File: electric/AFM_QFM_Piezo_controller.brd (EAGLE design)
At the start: 63.2 x 55.9 mm, 42 parts, among them U1 LTC3260EMSE#PBF, U2 AD5696RARUZ-RL7RU_16_ADI-M, U3 LM324KAD

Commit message: allboards
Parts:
- added C10, C12, C8: 10uF, SparkFun-Capacitors:0805
- added C11, C13, C9: 0.1uF, eagle-ltspice:C0805
- moved R8 6.35 mm to (33.0, 20.3)
- moved R9 6.35 mm to (29.2, 20.3)
- moved R18 5.24 mm to (22.9, 30.5)
- moved U$3 2.84 mm to (30.5, 25.4), turned to 90 degrees
- moved U$4 2.84 mm to (34.3, 25.4), turned to 90 degrees
- moved J2 2.54 mm to (2.54, 38.1)
- moved C2 1.27 mm to (39.4, 40.6)
- moved R1 1.27 mm to (48.3, 27.9)
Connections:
- removed net GROUND: C7.2, R4.1, U2.4
- removed net N$5: C2.2, J1.2, U1.1, U1.11, U1.13
- removed net VCC: C6.1, R3.2, U1.5, U3.11
- new net LDO+: C7.1, C8.1, C9.1, R14.2, R2.2, U1.12, U3.4
- new net LDO-: C10.1, C11.1, C6.1, R3.2, U1.5, U3.11
- net AGND: now also B1.GND@0, B1.GND@1, B1.GND@2, C10.2, C11.2, C12.2, C13.2, C7.2, C8.2, C9.2, J1.1, R4.1, U2.4; no longer J1.3, U2.10
- net VDD: now also C12.1, C13.1, C2.2, J1.2, U1.1, U1.11, U1.13, U2.10; no longer C7.1, R14.2, R2.2, U1.12, U3.4
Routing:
- net LDO-: track 0.00 -> 77.8 mm, vias 0 -> 2
- net VCC: track 69.7 -> 0.00 mm, vias 2 -> 0
- net N$5: track 48.3 -> 0.00 mm, vias 3 -> 0
- net LDO+: track 0.00 -> 38.1 mm, vias 0 -> 2
- net AGND: track 2.40 -> 27.1 mm, vias 0 -> 3
- net VDD: track 88.1 -> 98.2 mm, vias 3 -> 4
- net N$19: track 21.4 -> 28.5 mm
- net N$22: track 22.3 -> 27.4 mm
- net LDAC: track 34.2 -> 38.2 mm, vias 0 -> 2
- net VOUTB: track 16.9 -> 14.3 mm
- net P_OUT3: track 10.8 -> 13.3 mm
- net P_OUT4: track 29.1 -> 31.6 mm
- net N$24: track 8.44 -> 10.7 mm
- net N$2: track 3.81 -> 5.50 mm
- net N$9: track 9.67 -> 11.1 mm
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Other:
- board size 63.2 x 55.9 mm -> 64.4 x 55.9 mm

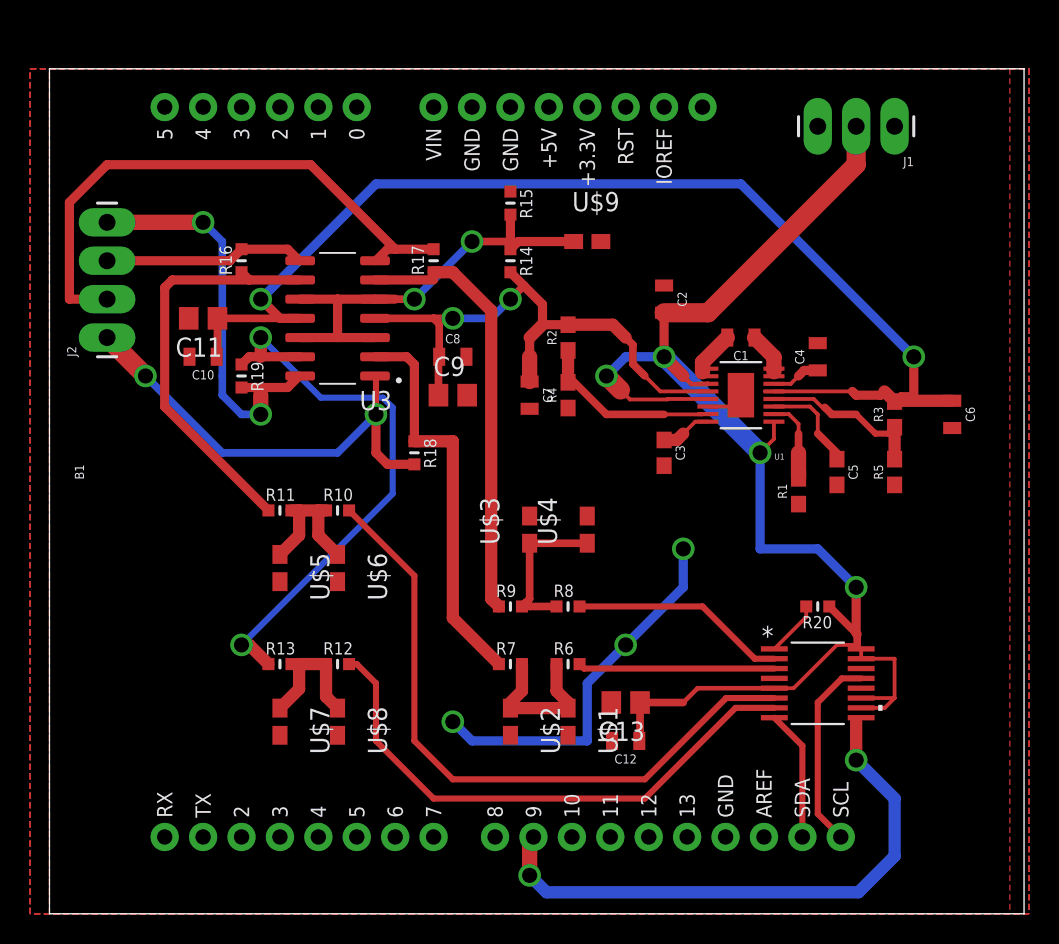
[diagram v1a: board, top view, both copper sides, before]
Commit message: Charge pump with his own power source
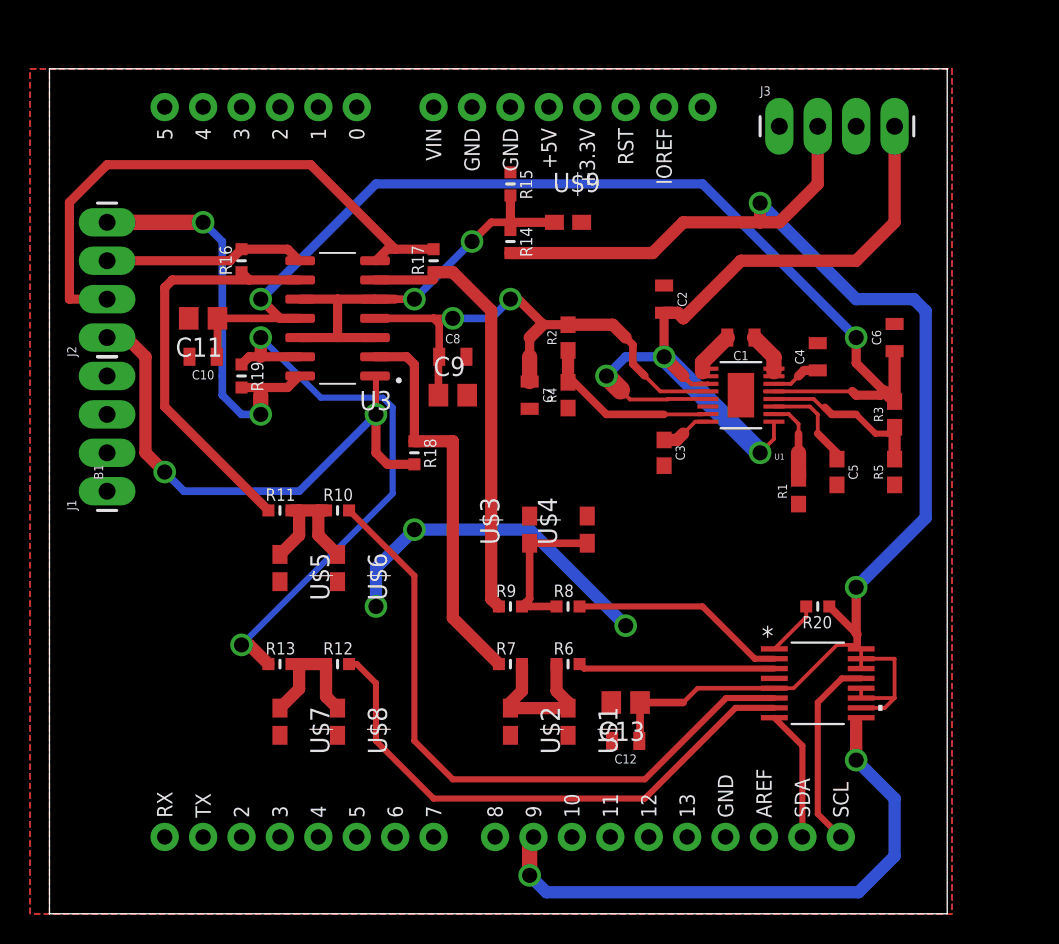
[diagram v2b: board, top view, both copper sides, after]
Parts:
- added J3: (no value), SparkFun-Connectors:1X04_LONGPADS
- J1: device SparkFun-Connectors:1X03_LONGPADS -> SparkFun-Connectors:1X04_LONGPADS
- moved J1 57.4 mm to (2.54, 27.9), turned to 90 degrees
- moved C6 6.35 mm to (54.6, 38.1), turned to 90 degrees
- moved U$9 1.80 mm to (33.0, 45.7)
- moved R14 1.27 mm to (29.2, 44.5)
- moved R15 1.27 mm to (29.2, 48.3)
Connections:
- new net V15+: C2.2, J3.4, U1.1, U1.11, U1.13
- net AGND: now also J1.2, J1.3, J1.4, J3.1; no longer U2.12, U2.14
- net LDO+: no longer R14.2
- net VDD: now also J3.2, R14.2, U2.12, U2.14; no longer C2.2, J1.2, U1.1, U1.11, U1.13
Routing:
- net V15+: track 0.00 -> 52.8 mm, vias 0 -> 3
- net P_OUT1: track 30.0 -> 35.8 mm
- net AGND: track 27.1 -> 22.7 mm
- net LDO-: track 77.8 -> 74.3 mm
- net LDO+: track 38.1 -> 35.6 mm
- net V_REF: track 29.3 -> 28.3 mm
- net N$3: track 2.79 -> 3.29 mm
- net VDD: track 98.2 -> 98.1 mm, vias 4 -> 2
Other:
- board size 64.4 x 55.9 mm -> 59.4 x 55.9 mm

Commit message: newer electroincs
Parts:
- J1: device SparkFun-Connectors:1X04_LONGPADS -> SparkFun-Connectors:1X01_LONGPAD
- moved J1 7.62 mm to (2.54, 35.6)
- moved J3 7.62 mm to (54.6, 52.1), turned to 180 degrees
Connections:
- net AGND: no longer J1.2, J1.3, J1.4
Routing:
- net V15+: track 52.8 -> 68.4 mm
- net VDD: track 98.1 -> 99.2 mm
- net N$22: track 27.4 -> 27.9 mm, vias 0 -> 1
- net N$16: track 26.4 -> 26.8 mm, vias 0 -> 1
- net N$19: vias 0 -> 1
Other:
- board size 59.4 x 55.9 mm -> 59.4 x 58.4 mm
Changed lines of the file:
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@@
 <plain>
 <wire x1="-1.27" y1="0" x2="58.09" y2="0" width="0" layer="20"/>
-<wire x1="58.09" y1="0" x2="58.09" y2="55.87" width="0" layer="20"/>
-<wire x1="58.09" y1="55.87" x2="-1.27" y2="55.87" width="0" layer="20"/>
-<wire x1="-1.27" y1="55.87" x2="-1.27" y2="0" width="0" layer="20"/>
+<wire x1="58.09" y1="0" x2="58.09" y2="58.41" width="0" layer="20"/>
+<wire x1="58.09" y1="58.41" x2="-1.27" y2="58.41" width="0" layer="20"/>
+<wire x1="-1.27" y1="58.41" x2="-1.27" y2="0" width="0" layer="20"/>
 </plain>
 <attributes>
@@
 <attribute name="VALUE" x="38.1" y="16.51" size="1.27" layer="27" rot="R180"/>
 </element>
-<element name="J3" library="SparkFun-Connectors" library_urn="urn:adsk.eagle:library:513" package="1X04_LONGPADS" package3d_urn="urn:adsk.eagle:package:38098/2" value="" x="46.99" y="52.07" smashed="yes">
-<attribute name="NAME" x="45.72" y="54.102" size="0.6096" layer="25" font="vector" ratio="20"/>
-<attribute name="PROD_ID" value="CONN-09696" x="46.99" y="52.07" size="1.778" layer="27" display="off"/>
-<attribute name="VALUE" x="45.72" y="49.403" size="0.6096" layer="27" font="vector" ratio="20"/>
-</element>
-<element name="J1" library="SparkFun-Connectors" library_urn="urn:adsk.eagle:library:513" package="1X04_LONGPADS" package3d_urn="urn:adsk.eagle:package:38098/2" value="" x="2.54" y="27.94" smashed="yes" rot="R90">
-<attribute name="NAME" x="0.508" y="26.67" size="0.6096" layer="25" font="vector" ratio="20" rot="R90"/>
-<attribute name="PROD_ID" value="CONN-09696" x="2.54" y="27.94" size="1.778" layer="27" rot="R90" display="off"/>
-<attribute name="VALUE" x="5.207" y="26.67" size="0.6096" layer="27" font="vector" ratio="20" rot="R90"/>
+<element name="J3" library="SparkFun-Connectors" library_urn="urn:adsk.eagle:library:513" package="1X04_LONGPADS" package3d_urn="urn:adsk.eagle:package:38098/2" value="" x="54.61" y="52.07" smashed="yes" rot="R180">
+<attribute name="NAME" x="55.88" y="50.038" size="0.6096" layer="25" font="vector" ratio="20" rot="R180"/>
+<attribute name="PROD_ID" value="CONN-09696" x="54.61" y="52.07" size="1.778" layer="27" rot="R180" display="off"/>
+<attribute name="VALUE" x="55.88" y="54.737" size="0.6096" layer="27" font="vector" ratio="20" rot="R180"/>
+</element>
+<element name="J1" library="SparkFun-Connectors" library_urn="urn:adsk.eagle:library:513" package="1X01_LONGPAD" package3d_urn="urn:adsk.eagle:package:38030/2" value="" x="2.54" y="35.56" smashed="yes" rot="R90">
+<attribute name="NAME" x="0.508" y="34.29" size="0.6096" layer="25" font="vector" ratio="20" rot="R90"/>
+<attribute name="VALUE" x="5.207" y="34.29" size="0.6096" layer="27" font="vector" ratio="20" rot="R90"/>
 </element>
 </elements>
@@
 <signal name="AGND">
 <polygon width="0.12" layer="1" spacing="1.9304" isolate="0.4064" orphans="yes" rank="6">
-<vertex x="-1.27" y="55.88"/>
-<vertex x="58.42" y="55.88"/>
+<vertex x="-1.27" y="58.42"/>
+<vertex x="58.42" y="58.42"/>
 <vertex x="58.42" y="0"/>
 <vertex x="-1.27" y="0"/>
@@
 <contactref element="C6" pad="2"/>
 <polygon width="0.508" layer="1">
-<vertex x="58.42" y="55.88"/>
+<vertex x="58.42" y="58.42"/>
 <vertex x="58.42" y="0"/>
 <vertex x="-2.54" y="0"/>
-<vertex x="-2.54" y="55.88"/>
+<vertex x="-2.54" y="58.42"/>
 </polygon>
 <polygon width="1.27" layer="1">
-<vertex x="58.42" y="55.88"/>
+<vertex x="58.42" y="58.42"/>
 <vertex x="58.42" y="0"/>
 <vertex x="-2.54" y="0"/>
-<vertex x="-2.54" y="55.88"/>
+<vertex x="-2.54" y="58.42"/>
 </polygon>
 <polygon width="1.27" layer="1" isolate="0.254">
-<vertex x="58.42" y="55.88"/>
+<vertex x="58.42" y="58.42"/>
 <vertex x="58.42" y="0"/>
 <vertex x="-2.54" y="0"/>
-<vertex x="-2.54" y="55.88"/>
+<vertex x="-2.54" y="58.42"/>
 </polygon>
 <polygon width="1.27" layer="1" isolate="0.4064">
-<vertex x="58.42" y="55.88"/>
+<vertex x="58.42" y="58.42"/>
 <vertex x="58.42" y="0"/>
 <vertex x="-2.54" y="0"/>
-<vertex x="-2.54" y="55.88"/>
+<vertex x="-2.54" y="58.42"/>
 </polygon>
 <contactref element="U$2" pad="2"/>
@@
 <contactref element="C12" pad="2"/>
 <contactref element="J3" pad="1"/>
-<contactref element="J1" pad="4"/>
-<contactref element="J1" pad="3"/>
-<contactref element="J1" pad="2"/>
-<contactref element="J1" pad="1"/>
 <via x="22.86" y="25.4" extent="1-16" drill="1"/>
 <via x="20.32" y="20.32" extent="1-16" drill="1"/>
@@
 <wire x1="22.86" y1="25.4" x2="30.48" y2="25.4" width="0.8128" layer="16"/>
 <wire x1="30.48" y1="25.4" x2="36.83" y2="19.05" width="0.8128" layer="16"/>
+<contactref element="J1" pad="1"/>
 <wire x1="44.45" y1="34.29" x2="42.2656" y2="33.53943125" width="0" layer="19" extent="1-1"/>
+<wire x1="39.37" y1="41.54" x2="42.2656" y2="33.53943125" width="0" layer="19" extent="1-1"/>
 </signal>
 <signal name="VDD">
@@
 <wire x1="52.4002" y1="16.215" x2="52.4002" y2="16.864996875" width="0.254" layer="1"/>
 <wire x1="52.4002" y1="14.915" x2="52.4002" y2="14.265" width="0.254" layer="1"/>
-<wire x1="46.99" y1="45.72" x2="49.53" y2="48.26" width="0.8128" layer="1"/>
 <wire x1="29.21" y1="43.688" x2="38.608" y2="43.688" width="0.8128" layer="1"/>
 <wire x1="38.608" y1="43.688" x2="40.64" y2="45.72" width="0.8128" layer="1"/>
 <wire x1="40.64" y1="45.72" x2="45.72" y2="45.72" width="0.8128" layer="1"/>
 <wire x1="45.72" y1="45.72" x2="46.99" y2="45.72" width="0.8128" layer="1"/>
-<wire x1="49.53" y1="48.26" x2="49.53" y2="52.07" width="0.8128" layer="1"/>
 <via x="45.72" y="46.99" extent="1-16" drill="1"/>
 <wire x1="45.72" y1="45.72" x2="45.72" y2="46.99" width="0.8128" layer="1"/>
@@
 <wire x1="56.6676" y1="26.1876" x2="52.07" y2="21.59" width="0.8128" layer="16"/>
 <wire x1="56.6676" y1="39.8524" x2="56.6676" y2="26.1876" width="0.8128" layer="16"/>
+<wire x1="46.99" y1="45.72" x2="52.07" y2="50.8" width="0.8128" layer="1"/>
+<wire x1="52.07" y1="50.8" x2="52.07" y2="52.07" width="0.8128" layer="1"/>
 </signal>
 <signal name="N$3">
@@
 <contactref element="U3" pad="2"/>
 <contactref element="R18" pad="1"/>
-<wire x1="25.4" y1="19.558" x2="28.448" y2="16.51" width="0.8128" layer="1"/>
+<wire x1="25.4" y1="19.558" x2="25.654" y2="19.304" width="0.8128" layer="1"/>
+<wire x1="25.654" y1="19.304" x2="28.448" y2="16.51" width="0.8128" layer="1"/>
 <wire x1="22.86" y1="31.242" x2="25.4" y2="31.242" width="0.8128" layer="1"/>
 <wire x1="25.4" y1="31.242" x2="25.4" y2="19.558" width="0.8128" layer="1"/>
@@
 <wire x1="22.86" y1="36.322" x2="22.352" y2="36.83" width="0.6096" layer="1"/>
 <wire x1="20.255" y1="36.83" x2="22.352" y2="36.83" width="0.6096" layer="1"/>
+<via x="25.4" y="19.05" extent="1-16" drill="1"/>
+<wire x1="25.4" y1="19.05" x2="25.654" y2="19.304" width="0.6096" layer="1"/>
 </signal>
 <signal name="VOUTB">
@@
 <wire x1="27.94" y1="39.878" x2="25.4" y2="42.418" width="0.8128" layer="1"/>
 <wire x1="25.4" y1="42.418" x2="24.13" y2="42.418" width="0.8128" layer="1"/>
-<wire x1="27.94" y1="20.828" x2="27.94" y2="39.878" width="0.8128" layer="1"/>
+<wire x1="27.94" y1="20.828" x2="27.94" y2="22.86" width="0.8128" layer="1"/>
+<wire x1="27.94" y1="22.86" x2="27.94" y2="39.878" width="0.8128" layer="1"/>
 <wire x1="20.255" y1="41.91" x2="24.13" y2="41.91" width="0.6096" layer="1"/>
+<via x="27.94" y="22.86" extent="1-16" drill="1"/>
 <wire x1="24.13" y1="42.418" x2="24.13" y2="41.91" width="0" layer="19" extent="1-1"/>
 </signal>
@@
 <wire x1="6.858" y1="41.91" x2="11.938" y2="41.91" width="0.6096" layer="1"/>
 <wire x1="11.938" y1="41.91" x2="15.24" y2="41.91" width="0.6096" layer="1"/>
-<wire x1="13.208" y1="26.67" x2="6.35" y2="33.528" width="0.6096" layer="1"/>
+<wire x1="13.208" y1="26.67" x2="9.779" y2="30.099" width="0.6096" layer="1"/>
+<wire x1="9.779" y1="30.099" x2="6.35" y2="33.528" width="0.6096" layer="1"/>
 <wire x1="6.35" y1="41.402" x2="6.858" y2="41.91" width="0.6096" layer="1"/>
 <wire x1="6.35" y1="33.528" x2="6.35" y2="41.402" width="0.6096" layer="1"/>
+<via x="10.16" y="30.48" extent="1-16" drill="1"/>
+<wire x1="10.16" y1="30.48" x2="9.779" y2="30.099" width="0.1524" layer="1"/>
 <wire x1="15.24" y1="41.91" x2="15.305" y2="41.91" width="0" layer="19" extent="1-1"/>
 </signal>
@@
 <wire x1="40.27" y1="39.74" x2="40.64" y2="39.37" width="0.8128" layer="1"/>
 <wire x1="44.45" y1="43.18" x2="52.07" y2="43.18" width="0.8128" layer="1"/>
-<wire x1="52.07" y1="43.18" x2="54.61" y2="45.72" width="0.8128" layer="1"/>
-<wire x1="54.61" y1="45.72" x2="54.61" y2="50.8" width="0.8128" layer="1"/>
 <wire x1="40.64" y1="39.37" x2="44.45" y2="43.18" width="0.8128" layer="1"/>
-<wire x1="54.61" y1="50.8" x2="54.61" y2="52.07" width="0" layer="19" extent="1-1"/>
+<wire x1="52.07" y1="43.18" x2="56.6676" y2="47.7776" width="0.8128" layer="1"/>
+<wire x1="56.6676" y1="47.7776" x2="56.6676" y2="53.66" width="0.8128" layer="1"/>
+<wire x1="55.7176" y1="54.61" x2="48.26" y2="54.61" width="0.8128" layer="1"/>
+<wire x1="48.26" y1="54.61" x2="46.99" y2="53.34" width="0.8128" layer="1"/>
+<wire x1="46.99" y1="53.34" x2="46.99" y2="52.07" width="0.8128" layer="1"/>
+<wire x1="56.6676" y1="53.66" x2="55.7176" y2="54.61" width="0.8128" layer="1"/>
 </signal>
 </signals>

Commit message: Updated to boards. Changes reflects fixes needed to PCBWay boards
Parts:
- 2R2, 2R3: value 100k -> 910k
- 2R4, 2R5: value 300k -> 100k
- renumbered B1 to 2B1, C1 to 2C1, C10 to 2C10, C11 to 2C11, C12 to 2C12, C13 to 2C13, C2 to 2C2, C3 to 2C3, C4 to 2C4, C5 to 2C5, C6 to 2C6, C7 to 2C7, C8 to 2C8, C9 to 2C9, J1 to 2J1, J2 to 2J2, J3 to 2J3, R1 to 2R1, R10 to 2R10, R11 to 2R11, R12 to 2R12, R13 to 2R13, R14 to 2R14, R15 to 2R15, R16 to 2R16, R17 to 2R17, R18 to 2R18, R19 to 2R19, R2 to 2R2, R20 to 2R20, R3 to 2R3, R4 to 2R4, R5 to 2R5, R6 to 2R6, R7 to 2R7, R8 to 2R8, R9 to 2R9, U$1 to 2U$1, U$2 to 2U$2, U$3 to 2U$3, U$4 to 2U$4, U$5 to 2U$5, U$6 to 2U$6, U$7 to 2U$7, U$8 to 2U$8, U$9 to 2U$9, U1 to 2U1, U2 to 2U2, U3 to 2U3
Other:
- board size 59.4 x 58.4 mm -> 60.6 x 58.4 mm
